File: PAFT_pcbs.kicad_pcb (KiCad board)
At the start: 4 copper layers, 65 x 56.5 mm, 41 parts, among them J1 Servo_R, J10 LinearPotR, J2 Servo_L, J3 Conn_02x03_Top_Bottom, J4 Actuator_L, J5 Actuator_R, J6 RPi_GPIO, J7 LinearPotL, J8 12V_In, J9 RPi_Terminal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

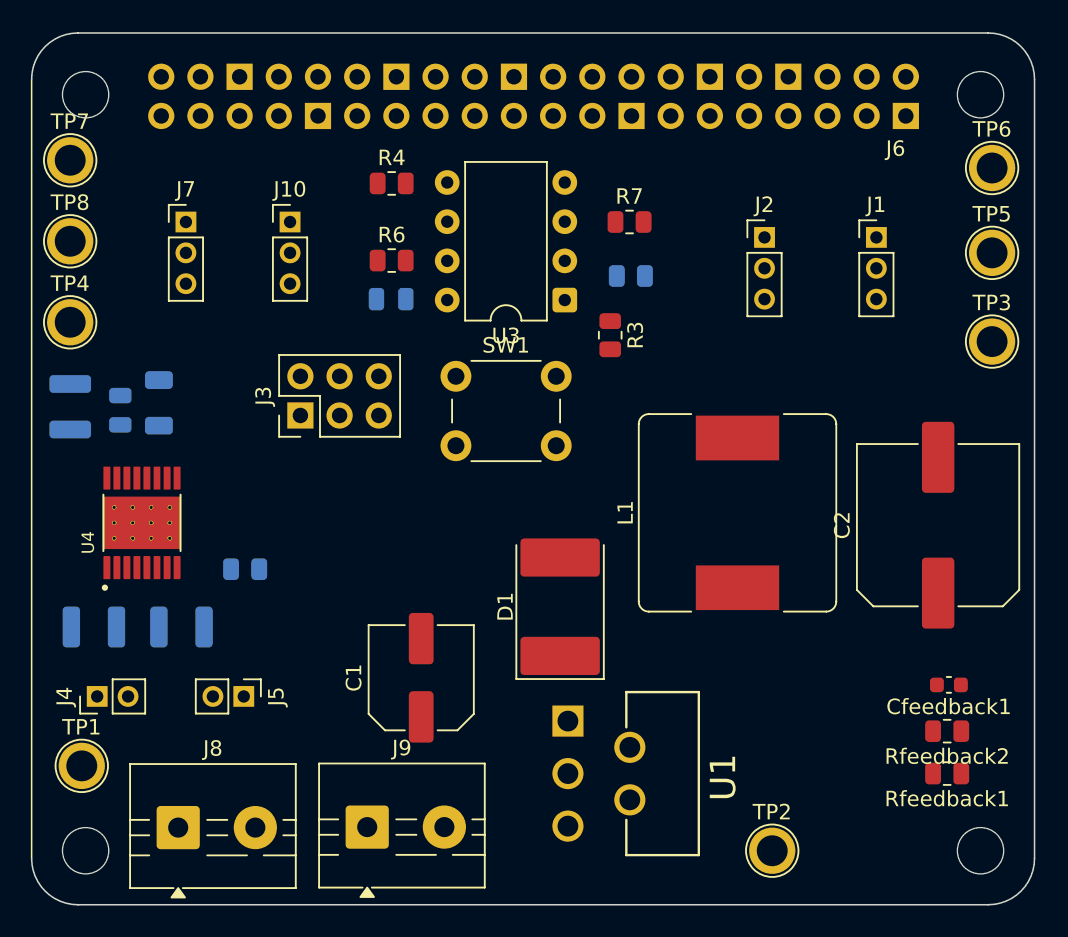
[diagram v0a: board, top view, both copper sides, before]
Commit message: PCB traces routed
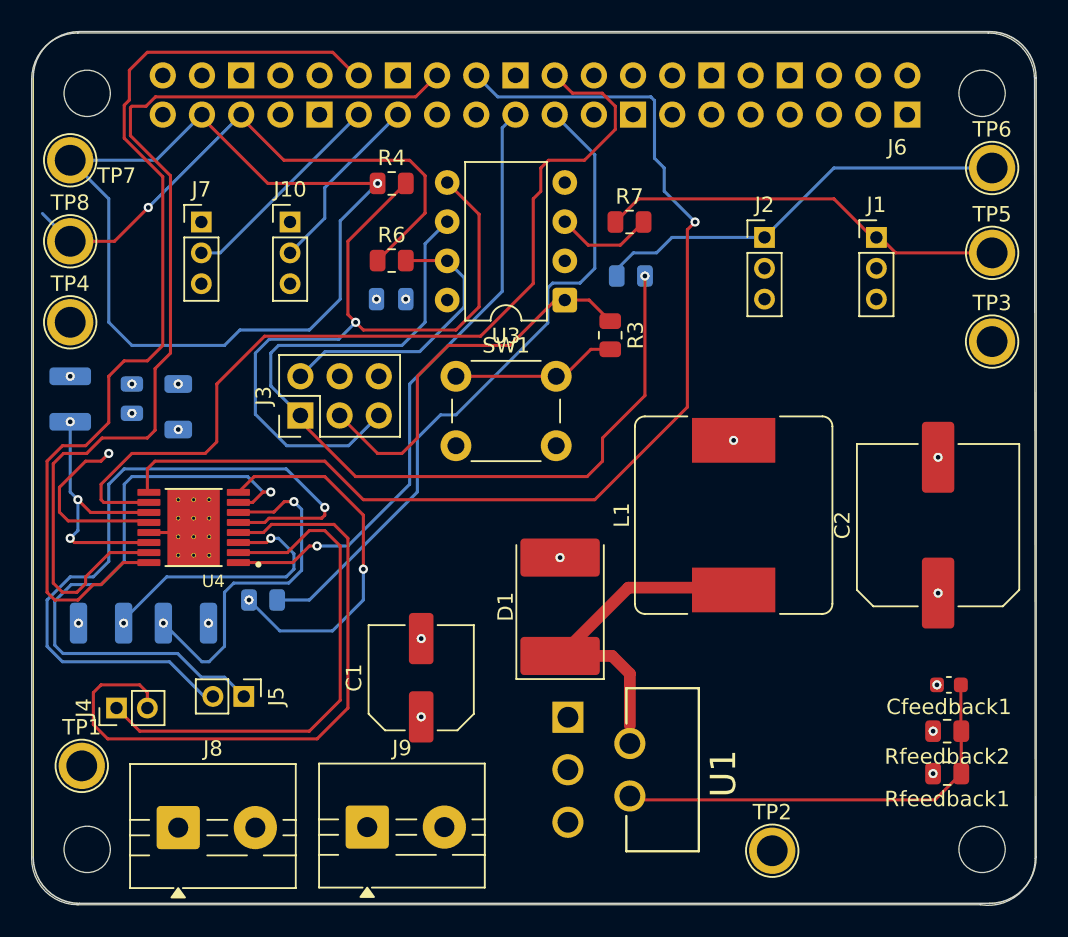
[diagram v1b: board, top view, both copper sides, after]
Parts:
- moved U4 3.36 mm to (79.5, 96.8), turned to 180 degrees
- moved 10kohm1 2.31 mm to (84.0, 101.5)
- moved J4 1.46 mm to (74.5, 108.5)
- moved 10uF1 1.27 mm to (78.5, 89.0)
- moved 0.1uF1 1.06 mm to (75.5, 88.5)
- moved J7 1.00 mm to (80.0, 77.0)
- moved 1.5ohms2 0.53 mm to (73.5, 103.0)
- moved 2.2uF1 0.50 mm to (71.5, 88.5)
- moved 1.5ohms1 0.38 mm to (79.0, 103.0)
- moved L1 0.29 mm to (114.5, 96.0)
- moved U1 0.25 mm to (116.0, 115.9)
- moved J6 0.13 mm to (101.6, 68.7)
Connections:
- U4 pad 18: (no net) -> GND
- U4 pad 19: (no net) -> GND
- U4 pad 20: (no net) -> GND
- U4 pad 21: (no net) -> GND
- U4 pad 22: (no net) -> GND
- U4 pad 23: (no net) -> GND
- U4 pad 24: (no net) -> GND
- U4 pad 25: (no net) -> GND
- U4 pad 26: (no net) -> GND
- U4 pad 27: (no net) -> GND
- U4 pad 28: (no net) -> GND
- U4 pad 29: (no net) -> GND
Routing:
- net /HBridge/BIN1: track 0.00 -> 73.7 mm, vias 0 -> 1
- net /HBridge/AIN2: track 0.00 -> 66.1 mm
- net /HBridge/AIN1: track 0.00 -> 63.6 mm
- net /ServoDriver/SDA: track 0.00 -> 60.5 mm, vias 0 -> 3
- net /HBridge/BIN2: track 0.00 -> 59.6 mm
- net Net-(J3-Pin_1): track 0.00 -> 57.8 mm, vias 0 -> 1
- net GND: track 0.00 -> 53.0 mm, vias 0 -> 24
- net Net-(J3-Pin_5): track 0.00 -> 49.5 mm, vias 0 -> 2
- net /HBridge/BOUT2: track 0.00 -> 46.9 mm, vias 0 -> 1
- net /HBridge/FAULT_N: track 0.00 -> 43.9 mm
- net /HBridge/AOUT2: track 0.00 -> 43.4 mm
- net /HBridge/BOUT1: track 0.00 -> 40.0 mm, vias 0 -> 1
- net /HBridge/SLEEP_N: track 0.00 -> 40.0 mm, vias 0 -> 1
- net /ServoDriver/SCL: track 0.00 -> 37.5 mm, vias 0 -> 1
- net /HBridge/AOUT1: track 0.00 -> 33.6 mm
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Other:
- outline, holes or cut-outs redrawn

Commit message: errors resolved
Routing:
- net +12V: track 27.7 -> 12.0 mm
- net /ServoDriver/SCL: track 37.5 -> 35.0 mm
- net /HBridge/AOUT2: track 43.4 -> 44.7 mm
- net Net-(U4-VINT): track 18.1 -> 17.1 mm
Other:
- outline, holes or cut-outs redrawn

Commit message: Routing adjustments
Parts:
- moved J3 5.77 mm to (91.6, 87.0), turned to -90 degrees
- moved R6 4.32 mm to (93.4, 75.3), turned to -90 degrees
- moved R4 2.10 mm to (90.4, 75.3), turned to -90 degrees
- moved J4 2.00 mm to (76.5, 108.4), turned to -90 degrees
- moved R3 0.70 mm to (105.8, 84.3)
- moved R5 0.11 mm to (107.9, 80.6), turned to 180 degrees
- turned R7 to 180 degrees
- renumbered Cfeedback1 to Cf1, Rfeedback1 to Rf1, Rfeedback2 to Rf2
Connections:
- J6 pad 14: unconnected-(J6-GND-Pad14) -> GND
- J6 pad 20: unconnected-(J6-GND-Pad20) -> GND
- J6 pad 25: unconnected-(J6-GND-Pad25) -> GND
- J6 pad 30: unconnected-(J6-GND-Pad30) -> GND
- J6 pad 34: unconnected-(J6-GND-Pad34) -> GND
- J6 pad 4: unconnected-(J6-5V-Pad4) -> +5V
- J6 pad 6: unconnected-(J6-GND-Pad6) -> GND
- J6 pad 9: unconnected-(J6-GND-Pad9) -> GND
- U3 pad 2: unconnected-(U3-XTAL1/PB3-Pad2) -> GND
- U4 pad 18: GND -> (no net)
- U4 pad 19: GND -> (no net)
- U4 pad 20: GND -> (no net)
- U4 pad 21: GND -> (no net)
- U4 pad 22: GND -> (no net)
- U4 pad 23: GND -> (no net)
- U4 pad 24: GND -> (no net)
- U4 pad 25: GND -> (no net)
- U4 pad 26: GND -> (no net)
- U4 pad 27: GND -> (no net)
- U4 pad 28: GND -> (no net)
- U4 pad 29: GND -> (no net)
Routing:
- net /ServoDriver/SDA: track 60.5 -> 22.6 mm, vias 3 -> 0
- net /HBridge/BIN1: track 73.7 -> 37.7 mm
- net Net-(J3-Pin_1): track 57.8 -> 36.7 mm
- net Net-(J3-Pin_5): track 49.5 -> 30.6 mm, vias 2 -> 1
- net /HBridge/AIN2: track 66.1 -> 57.5 mm
- net +12V: track 12.0 -> 3.34 mm
- net /HBridge/BIN2: track 59.6 -> 51.3 mm
- net /HBridge/AOUT2: track 44.7 -> 36.7 mm
- net GND: track 53.0 -> 45.1 mm, vias 24 -> 10
- net /ServoDriver/SCL: track 35.0 -> 27.5 mm, vias 1 -> 0
- net /HBridge/AIN1: track 63.6 -> 56.4 mm
- net Net-(J3-Pin_3): track 25.6 -> 19.4 mm
- net Net-(U3-XTAL2/PB4): track 6.36 -> 3.29 mm
- net /HBridge/AOUT1: track 33.1 -> 31.2 mm
- net /ServoDriver/PWM_R: track 26.5 -> 24.7 mm
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
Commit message: Fixed DRC errors
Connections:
- U4 pad 18: (no net) -> GND
- U4 pad 19: (no net) -> GND
- U4 pad 20: (no net) -> GND
- U4 pad 21: (no net) -> GND
- U4 pad 22: (no net) -> GND
- U4 pad 23: (no net) -> GND
- U4 pad 24: (no net) -> GND
- U4 pad 25: (no net) -> GND
- U4 pad 26: (no net) -> GND
- U4 pad 27: (no net) -> GND
- U4 pad 28: (no net) -> GND
- U4 pad 29: (no net) -> GND
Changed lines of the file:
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@@
 			(size 0.3 0.3)
 			(drill 0.2)
+			(property pad_prop_heatsink)
 			(layers "*.Cu")
 			(remove_unused_layers no)
+			(net 1 "GND")
 		)
 		(pad "19" thru_hole circle
@@
 			(size 0.3 0.3)
 			(drill 0.2)
+			(property pad_prop_heatsink)
 			(layers "*.Cu")
 			(remove_unused_layers no)
+			(net 1 "GND")
 		)
 		(pad "20" thru_hole circle
@@
 			(size 0.3 0.3)
 			(drill 0.2)
+			(property pad_prop_heatsink)
 			(layers "*.Cu")
 			(remove_unused_layers no)
+			(net 1 "GND")
 		)
 		(pad "21" thru_hole circle
@@
 			(size 0.3 0.3)
 			(drill 0.2)
+			(property pad_prop_heatsink)
 			(layers "*.Cu")
 			(remove_unused_layers no)
+			(net 1 "GND")
 		)
 		(pad "22" thru_hole circle
@@
 			(size 0.3 0.3)
 			(drill 0.2)
+			(property pad_prop_heatsink)
 			(layers "*.Cu")
 			(remove_unused_layers no)
+			(net 1 "GND")
 		)
 		(pad "23" thru_hole circle
@@
 			(size 0.3 0.3)
 			(drill 0.2)
+			(property pad_prop_heatsink)
 			(layers "*.Cu")
 			(remove_unused_layers no)
+			(net 1 "GND")
 		)
 		(pad "24" thru_hole circle
@@
 			(size 0.3 0.3)
 			(drill 0.2)
+			(property pad_prop_heatsink)
 			(layers "*.Cu")
 			(remove_unused_layers no)
+			(net 1 "GND")
 		)
 		(pad "25" thru_hole circle
@@
 			(size 0.3 0.3)
 			(drill 0.2)
+			(property pad_prop_heatsink)
 			(layers "*.Cu")
 			(remove_unused_layers no)
+			(net 1 "GND")
 		)
 		(pad "26" thru_hole circle
@@
 			(size 0.3 0.3)
 			(drill 0.2)
+			(property pad_prop_heatsink)
 			(layers "*.Cu")
 			(remove_unused_layers no)
+			(net 1 "GND")
 		)
 		(pad "27" thru_hole circle
@@
 			(size 0.3 0.3)
 			(drill 0.2)
+			(property pad_prop_heatsink)
 			(layers "*.Cu")
 			(remove_unused_layers no)
+			(net 1 "GND")
 		)
 		(pad "28" thru_hole circle
@@
 			(size 0.3 0.3)
 			(drill 0.2)
+			(property pad_prop_heatsink)
 			(layers "*.Cu")
 			(remove_unused_layers no)
+			(net 1 "GND")
 		)
 		(pad "29" thru_hole circle
@@
 			(size 0.3 0.3)
 			(drill 0.2)
+			(property pad_prop_heatsink)
 			(layers "*.Cu")
 			(remove_unused_layers no)
+			(net 1 "GND")
 		)
 		(embedded_fonts no)

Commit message: Routing updates
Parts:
- 10kohm1: moved to F.Cu
- moved 10kohm1 8.56 mm to (85.0, 93.0)
- moved J5 2.35 mm to (85.1, 107.8)
- moved 1.5ohms1 1.04 mm to (80.0, 103.0), turned to 0 degrees
- moved J4 0.61 mm to (76.4, 107.8), turned to 90 degrees
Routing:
- net GND: track 45.1 -> 3.42 mm
- net /HBridge/BOUT2: track 46.9 -> 15.5 mm, vias 1 -> 0
- net /HBridge/BOUT1: track 39.6 -> 16.4 mm, vias 1 -> 0
- net Net-(U4-FAULT_N): track 24.7 -> 2.33 mm, vias 1 -> 0
- net /HBridge/AOUT2: track 36.7 -> 17.4 mm
- net /HBridge/AOUT1: track 31.2 -> 16.8 mm
- net Net-(U4-BISEN): track 23.0 -> 10.3 mm
- net /HBridge/FAULT_N: track 43.9 -> 37.6 mm, vias 0 -> 1
- net Net-(U4-AISEN): track 17.7 -> 13.0 mm
- net Net-(U4-VINT): track 17.1 -> 18.4 mm
- net Net-(J3-Pin_5): track 30.6 -> 31.2 mm

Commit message: Final updates
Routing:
- net /HBridge/BOUT1: track 16.4 -> 18.1 mm
- net /HBridge/AOUT2: track 17.4 -> 18.5 mm
- net /HBridge/BOUT2: track 15.5 -> 16.5 mm
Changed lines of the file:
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@@
 		)
 		(pad_to_mask_clearance 0)
-		(solder_mask_min_width 0.0762)
 		(allow_soldermask_bridges_in_footprints no)
 		(tenting front back)
@@
 			(outputformat 1)
 			(mirror no)
-			(drillshape 1)
+			(drillshape 0)
 			(scaleselection 1)
-			(outputdirectory "")
+			(outputdirectory "../Downloads/")
 		)
 	)
@@
 	)
 	(segment
-		(start 82.3 105)
-		(end 85.2 102.1)
-		(width 0.2)
+		(start 79.2 105)
+		(end 82.3 105)
+		(width 0.25)
 		(layer "F.Cu")
 		(net 18)
 	)
 	(segment
-		(start 85.2 99.8)
-		(end 83.825 98.425)
-		(width 0.2)
+		(start 76.4 107.8)
+		(end 79.2 105)
+		(width 0.25)
 		(layer "F.Cu")
 		(net 18)
 	)
 	(segment
-		(start 83.825 98.425)
-		(end 82.4 98.425)
-		(width 0.2)
+		(start 82.3 105)
+		(end 85.2 102.1)
+		(width 0.25)
 		(layer "F.Cu")
 		(net 18)
 	)
 	(segment
-		(start 85.2 102.1)
-		(end 85.2 99.8)
-		(width 0.2)
+		(start 83.182328 98.425)
+		(end 82.4 98.425)
+		(width 0.25)
 		(layer "F.Cu")
 		(net 18)
 	)
 	(segment
-		(start 79.2 105)
-		(end 82.3 105)
-		(width 0.2)
+		(start 85.2 100.442672)
+		(end 83.182328 98.425)
+		(width 0.25)
 		(layer "F.Cu")
 		(net 18)
 	)
 	(segment
-		(start 76.4 107.8)
-		(end 79.2 105)
-		(width 0.2)
+		(start 85.2 102.1)
+		(end 85.2 100.442672)
+		(width 0.25)
 		(layer "F.Cu")
 		(net 18)
 	)
 	(segment
-		(start 84.825 97.125)
-		(end 85.6 97.9)
-		(width 0.2)
+		(start 86.5 99)
+		(end 86.5 102.2)
+		(width 0.25)
 		(layer "F.Cu")
 		(net 19)
 	)
 	(segment
-		(start 80.1 107.8)
+		(start 80.9 107.8)
 		(end 78.4 107.8)
-		(width 0.2)
+		(width 0.25)
 		(layer "F.Cu")
 		(net 19)
 	)
 	(segment
-		(start 85.6 97.9)
-		(end 85.6 102.3)
-		(width 0.2)
+		(start 86.5 102.2)
+		(end 80.9 107.8)
+		(width 0.25)
 		(layer "F.Cu")
 		(net 19)
 	)
 	(segment
-		(start 85.6 102.3)
-		(end 80.1 107.8)
-		(width 0.2)
+		(start 82.4 97.125)
+		(end 84.625 97.125)
+		(width 0.25)
 		(layer "F.Cu")
 		(net 19)
 	)
 	(segment
-		(start 82.4 97.125)
-		(end 84.825 97.125)
-		(width 0.2)
+		(start 84.625 97.125)
+		(end 86.5 99)
+		(width 0.25)
 		(layer "F.Cu")
 		(net 19)
 	)
 	(segment
-		(start 84.775 95.175)
-		(end 82.4 95.175)
-		(width 0.2)
+		(start 82.4 95.175)
+		(end 83.182328 95.175)
+		(width 0.25)
 		(layer "F.Cu")
 		(net 20)
 	)
 	(segment
-		(start 85.1 107.8)
-		(end 86.6 106.3)
-		(width 0.2)
+		(start 83.557328 94.8)
+		(end 84.7 94.8)
+		(width 0.25)
 		(layer "F.Cu")
 		(net 20)
 	)
 	(segment
-		(start 86.6 97)
-		(end 84.775 95.175)
-		(width 0.2)
+		(start 88.1 98.2)
+		(end 88.1 104.8)
+		(width 0.25)
 		(layer "F.Cu")
 		(net 20)
 	)
 	(segment
-		(start 86.6 106.3)
-		(end 86.6 97)
-		(width 0.2)
+		(start 83.182328 95.175)
+		(end 83.557328 94.8)
+		(width 0.25)
 		(layer "F.Cu")
 		(net 20)
 	)
 	(segment
-		(start 86.101 97.8339)
-		(end 84.7421 96.475)
-		(width 0.2)
+		(start 88.1 104.8)
+		(end 85.1 107.8)
+		(width 0.25)
 		(layer "F.Cu")
-		(net 21)
+		(net 20)
 	)
 	(segment
-		(start 86.1 104.8)
-		(end 86.1 97.8349)
-		(width 0.2)
+		(start 84.7 94.8)
+		(end 88.1 98.2)
+		(width 0.25)
+		(layer "F.Cu")
+		(net 20)
+	)
+	(segment
+		(start 84.975 96.475)
+		(end 82.4 96.475)
+		(width 0.25)
 		(layer "F.Cu")
 		(net 21)
 	)
 	(segment
-		(start 86.1 97.8349)
-		(end 86.101 97.8339)
-		(width 0.2)
+		(start 83.1 107.8)
+		(end 87.2 103.7)
+		(width 0.25)
 		(layer "F.Cu")
 		(net 21)
 	)
 	(segment
-		(start 84.7421 96.475)
-		(end 82.4 96.475)
-		(width 0.2)
+		(start 87.2 98.7)
+		(end 84.975 96.475)
+		(width 0.25)
 		(layer "F.Cu")
 		(net 21)
 	)
 	(segment
-		(start 83.1 107.8)
-		(end 86.1 104.8)
-		(width 0.2)
+		(start 87.2 103.7)
+		(end 87.2 98.7)
+		(width 0.25)
 		(layer "F.Cu")
 		(net 21)
